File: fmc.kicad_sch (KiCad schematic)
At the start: 3 parts, among them J1 SAMTEC_ASP-134604-01, U1 M24C02-FMN

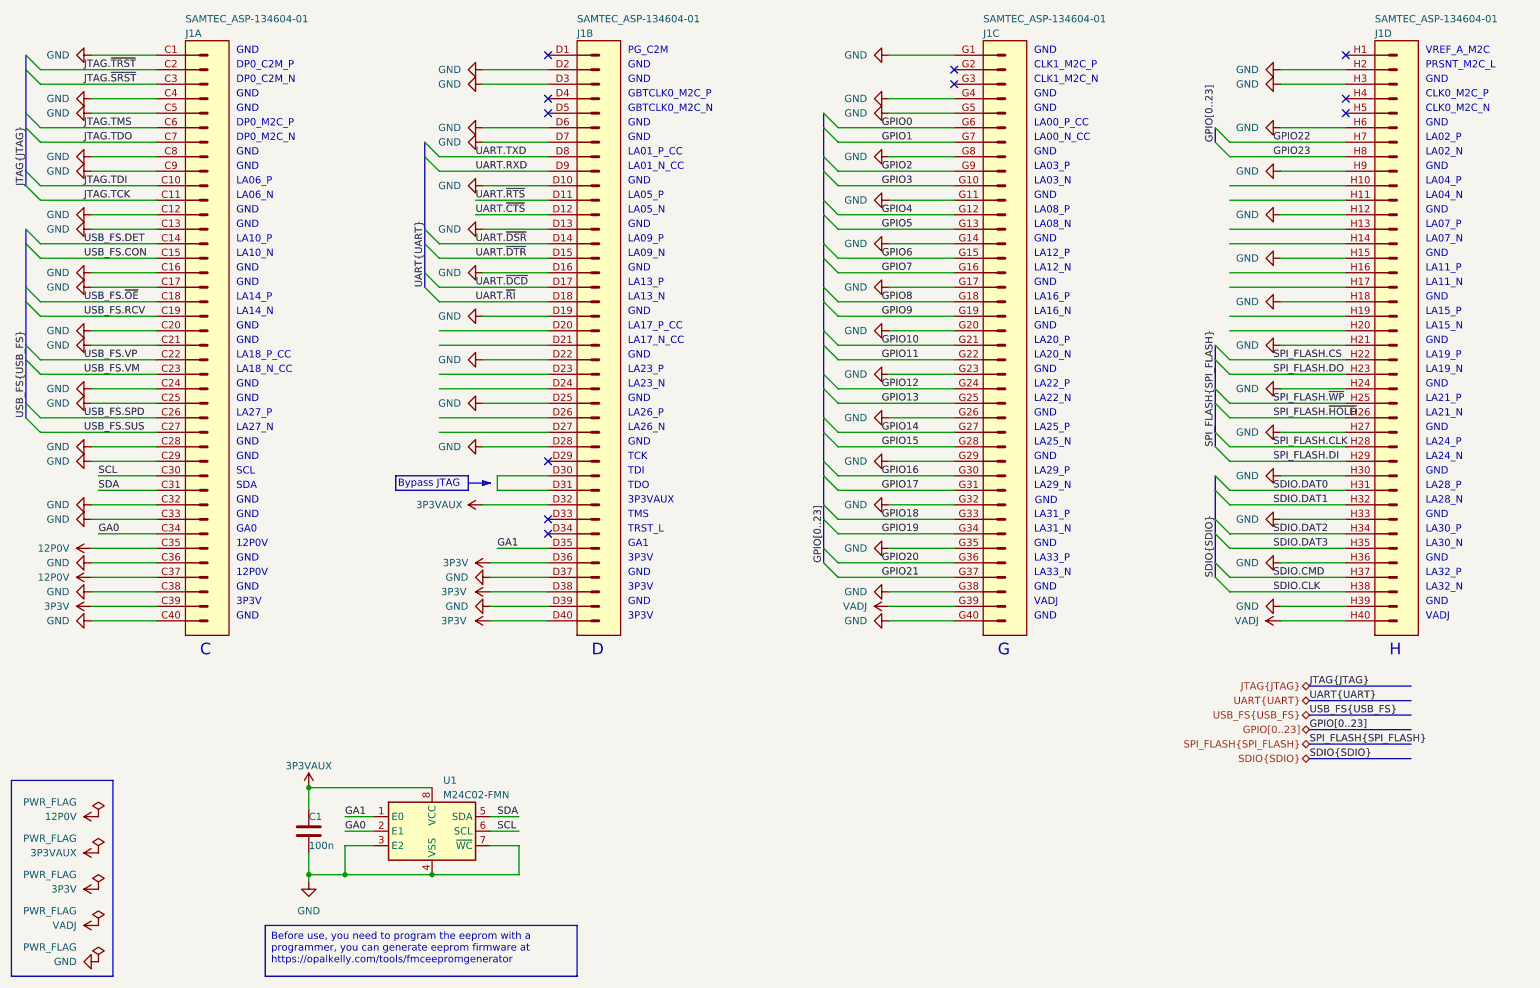
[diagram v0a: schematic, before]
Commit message: fmc.kicad_sch: finished all bus label connection
Signed-off-by: Huang Rui <vowstar@gmail.com>
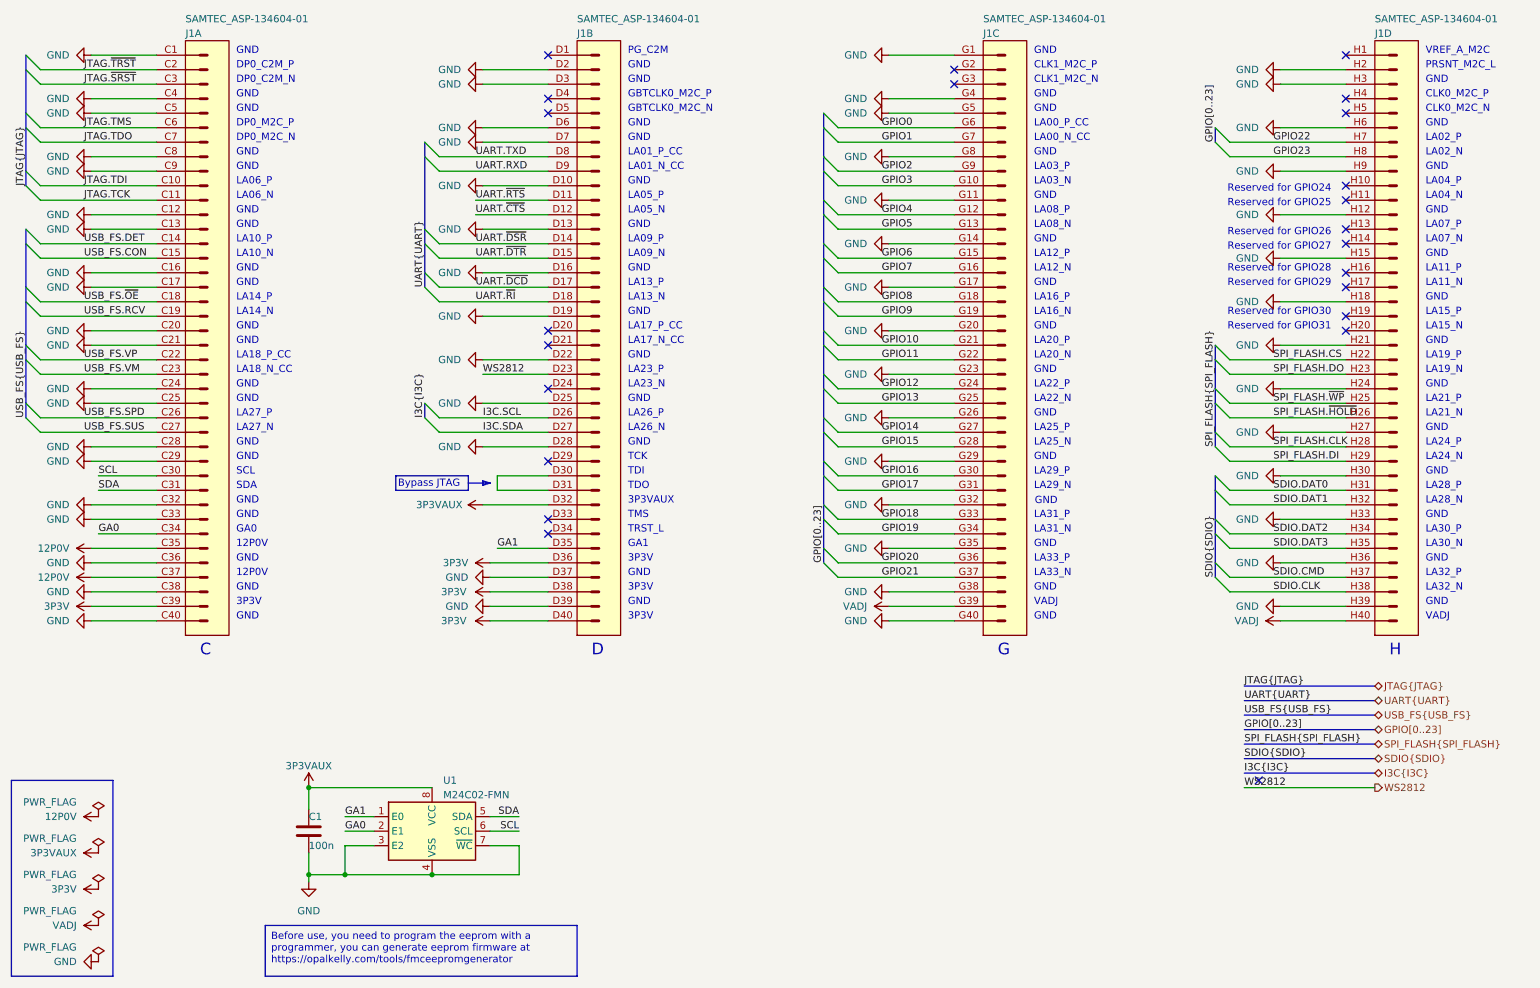
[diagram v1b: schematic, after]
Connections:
- net WS2812: now reaches J1.D23 (d23)
- net I3C.SCL: now reaches J1.D26 (d26)
- net I3C.SDA: now reaches J1.D27 (d27)
- no-connect marks 11 -> 23
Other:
- note added: "Reserved for GPIO24"
- note added: "Reserved for GPIO25"
- note added: "Reserved for GPIO26"
- note added: "Reserved for GPIO27"
- note added: "Reserved for GPIO28"
- note added: "Reserved for GPIO29"
- note added: "Reserved for GPIO30"
- note added: "Reserved for GPIO31"

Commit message: *.kicad_sch: ERC clean
Signed-off-by: Huang Rui <vowstar@gmail.com>
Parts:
- J1: footprint Connector:Samtec_FMC_ASP-134604-01_4x40_P1.27mm -> CHIPSAlliance_Connector:Samtec_FMC_ASP-134604-01_4x40_P1.27mm
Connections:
- net SPI_FLASH.CS renamed SPI_FLASH.~{CS}
- no-connect marks 23 -> 22
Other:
- moved on the sheet: C1, U1

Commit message: {library,*.kicad_sch}: fix power symbols, ERC clean
Signed-off-by: Huang Rui <vowstar@gmail.com>
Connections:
- removed net VDD: C1.1, J1.C35 (Pin_35), J1.C37 (Pin_37), J1.C39 (Pin_39), J1.D32 (d32), J1.D36 (d36), J1.D38 (d38), J1.D40 (d40), J1.G39 (g39), J1.H40 (h40), U1.8 (VCC)
- new net 12P0V: J1.C35 (Pin_35), J1.C37 (Pin_37)
- new net 3P3V: J1.C39 (Pin_39), J1.D36 (d36), J1.D38 (d38), J1.D40 (d40)
- new net 3P3VAUX: C1.1, J1.D32 (d32), U1.8 (VCC)
- new net VADJ: J1.G39 (g39), J1.H40 (h40)

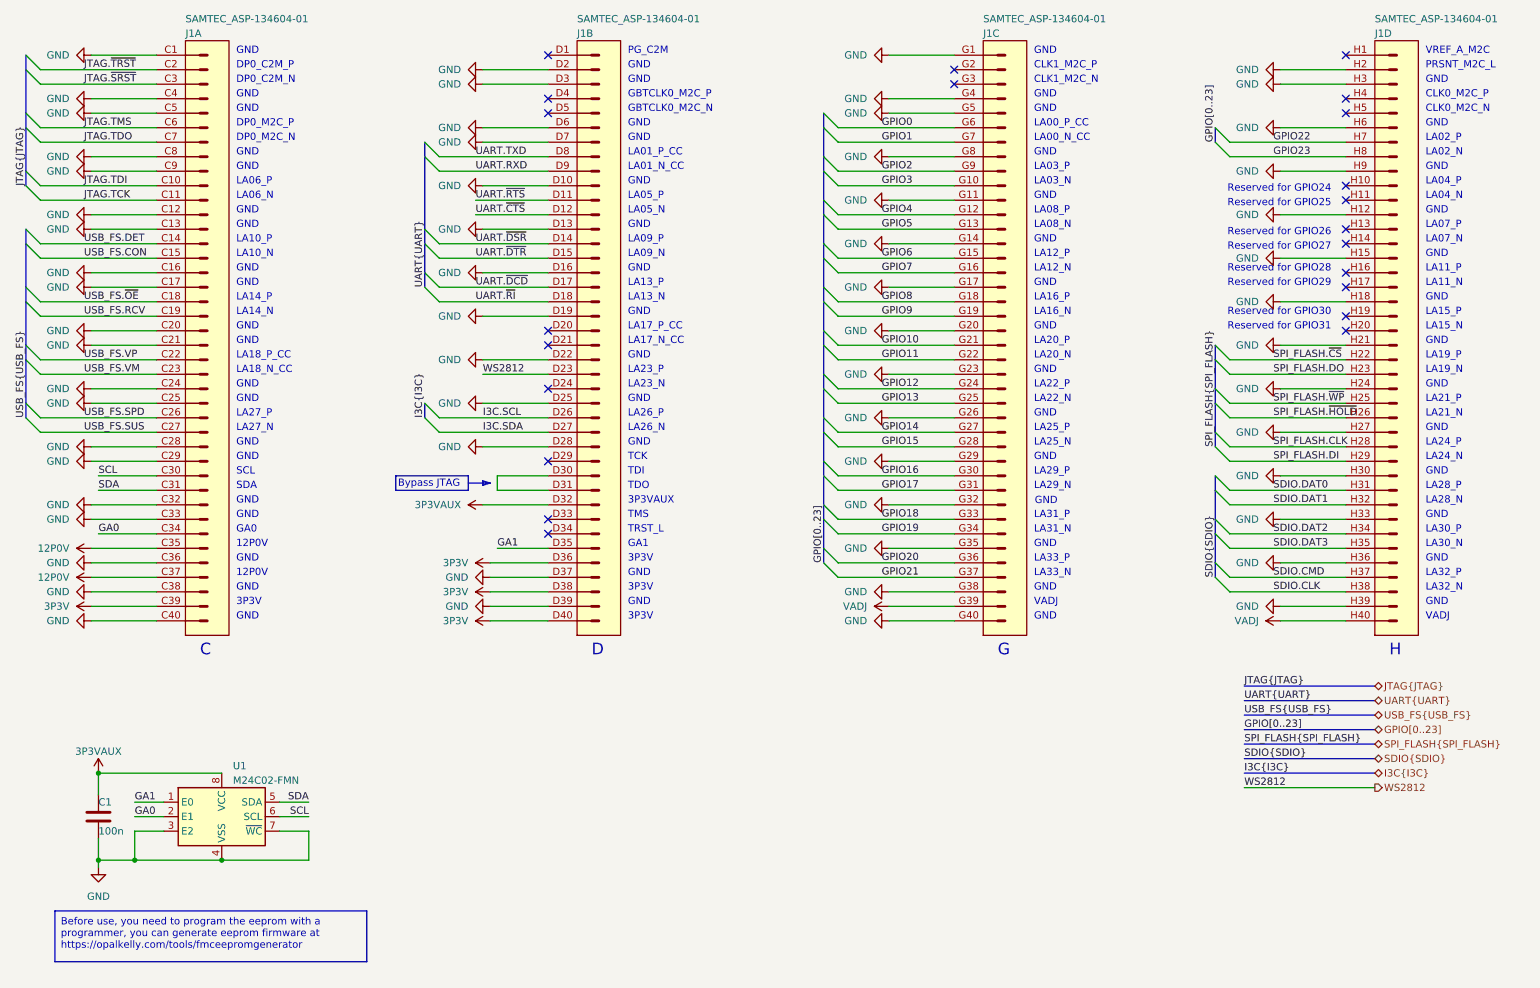
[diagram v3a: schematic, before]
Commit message: *.kicad_sch: expand gpio to [0..31]
Signed-off-by: Huang Rui <vowstar@gmail.com>
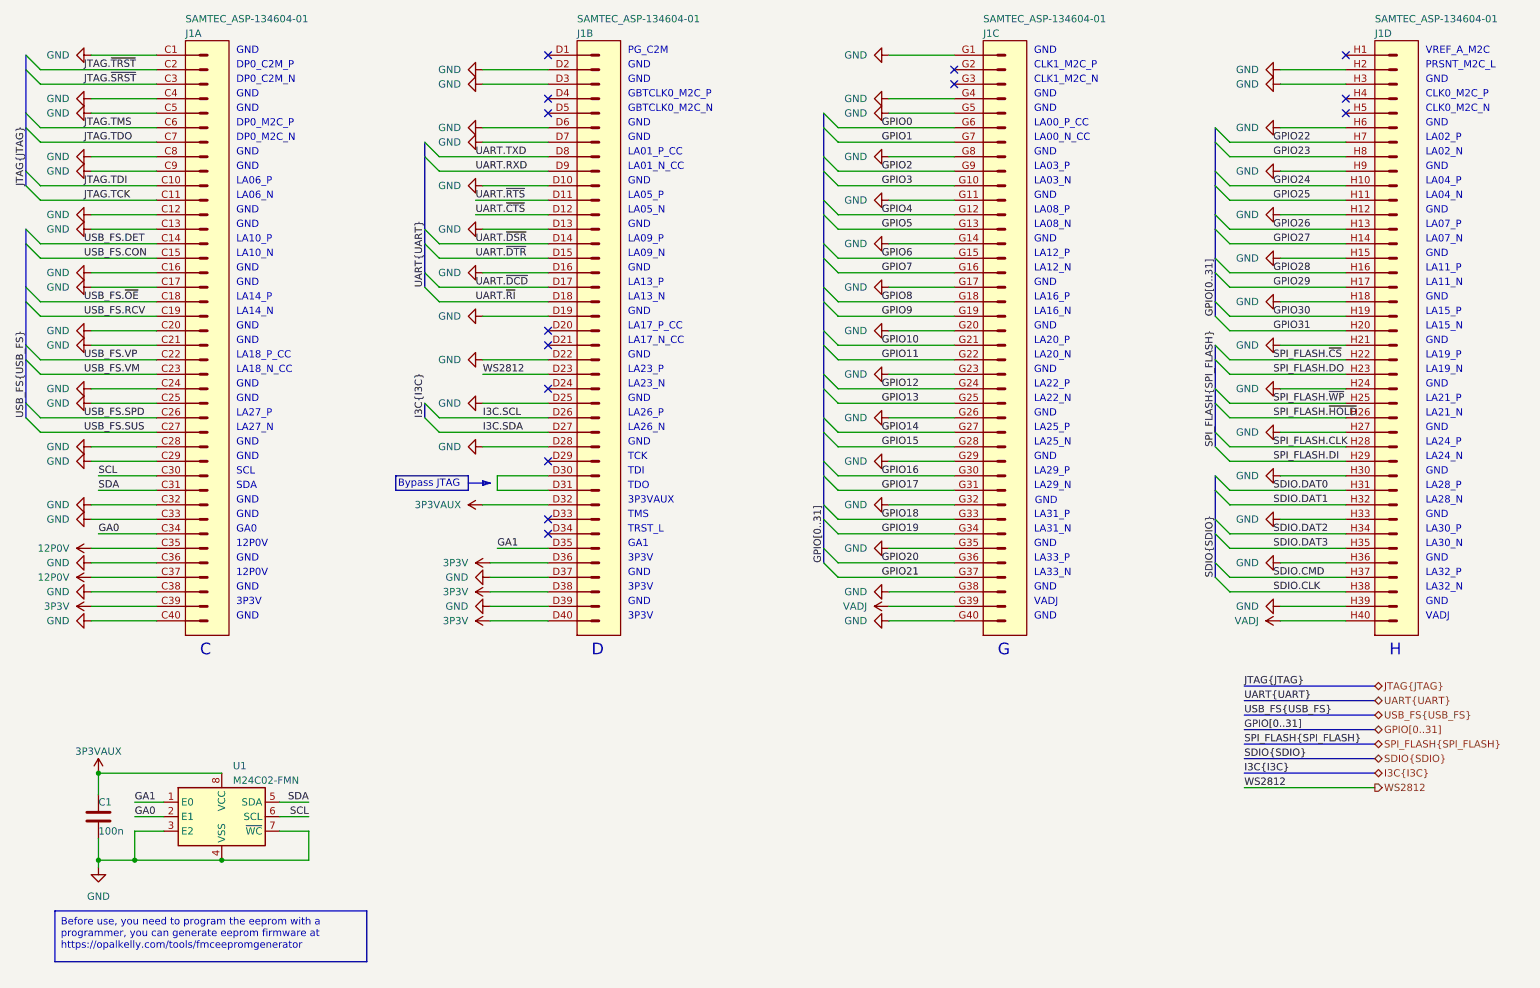
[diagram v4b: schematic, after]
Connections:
- net GPIO24: now reaches J1.H10 (h10)
- net GPIO25: now reaches J1.H11 (h11)
- net GPIO26: now reaches J1.H13 (h13)
- net GPIO27: now reaches J1.H14 (h14)
- net GPIO28: now reaches J1.H16 (h16)
- net GPIO29: now reaches J1.H17 (h17)
- net GPIO30: now reaches J1.H19 (h19)
- net GPIO31: now reaches J1.H20 (h20)
- no-connect marks 22 -> 14
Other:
- note removed: "Reserved for GPIO24"
- note removed: "Reserved for GPIO25"
- note removed: "Reserved for GPIO26"
- note removed: "Reserved for GPIO27"
- note removed: "Reserved for GPIO28"
- note removed: "Reserved for GPIO29"
- note removed: "Reserved for GPIO30"
- note removed: "Reserved for GPIO31"

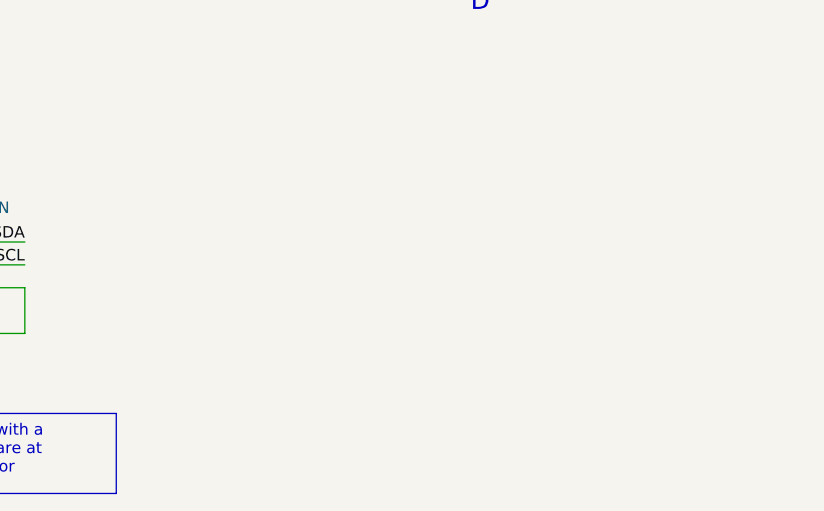
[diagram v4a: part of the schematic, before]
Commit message: *.kicad_sch: add more detailed annotations for signals
Signed-off-by: Huang Rui <vowstar@gmail.com>
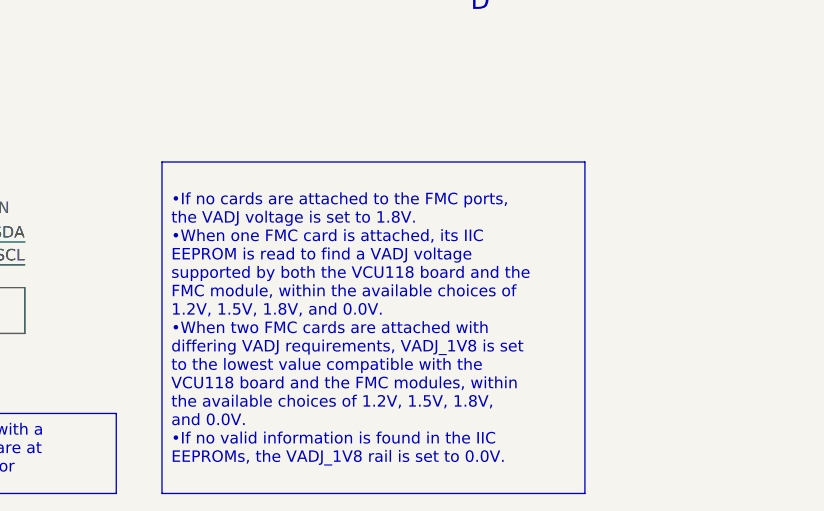
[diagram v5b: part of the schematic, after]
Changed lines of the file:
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@@
     (stroke (width 0) (type default))
+  )
+  (text_box "•If no cards are attached to the FMC ports, the VADJ voltage is set to 1.8V.\n•When one FMC card is attached, its IIC EEPROM is read to find a VADJ voltage supported by both the VCU118 board and the FMC module, within the available choices of 1.2V, 1.5V, 1.8V, and 0.0V.\n•When two FMC cards are attached with differing VADJ requirements, VADJ_1V8 is set to the lowest value compatible with the VCU118 board and the FMC modules, within the available choices of 1.2V, 1.5V, 1.8V, and 0.0V.\n•If no valid information is found in the IIC EEPROMs, the VADJ_1V8 rail is set to 0.0V."
+    (at 87.63 149.86 0) (size 46.99 36.83)
+    (stroke (width 0) (type default))
+    (fill (type none))
+    (effects (font (size 1.27 1.27)) (justify left))
   )
   (text_box "Before use, you need to program the eeprom with a programmer, you can generate eeprom firmware at\nhttps://opalkelly.com/tools/fmceepromgenerator"
